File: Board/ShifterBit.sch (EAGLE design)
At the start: 10 parts, among them P1 PINHD-1X10, P2 PINHD-1X10

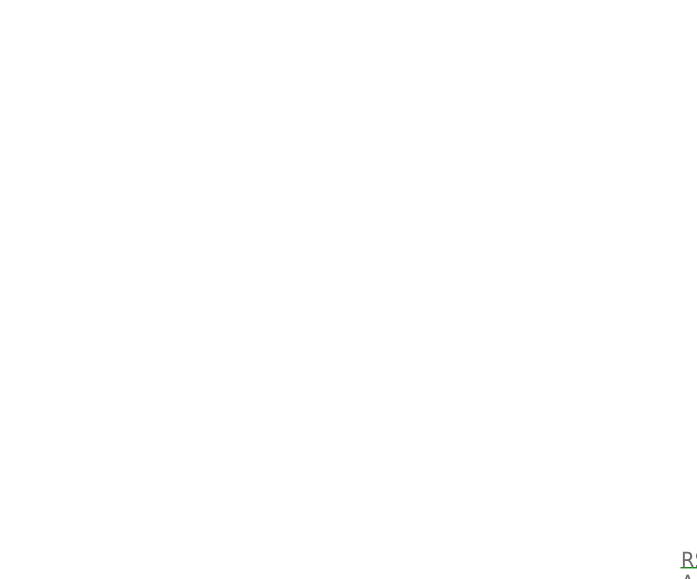
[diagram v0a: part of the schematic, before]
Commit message: renamed and added voltage divider for signal input
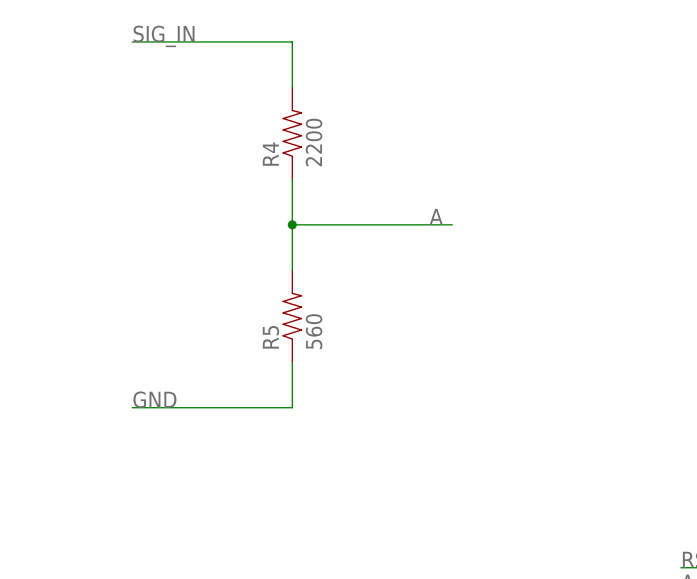
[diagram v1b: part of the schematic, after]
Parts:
- added R4: 2200, SparkFun-Passives:RESISTOR0603-RES
- added R5: 560, SparkFun-Passives:RESISTOR0603-RES
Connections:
- net A: now also R4.1, R5.2
- net GND: now also R5.1
- net SIG_IN: now also R4.2
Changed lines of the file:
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@@
 <part name="R2" library="SparkFun-Passives" deviceset="RESISTOR" device="0603-RES" value="56"/>
 <part name="R3" library="SparkFun-Passives" deviceset="RESISTOR" device="0603-RES" value="56"/>
+<part name="R4" library="SparkFun-Passives" deviceset="RESISTOR" device="0603-RES" value="2200"/>
+<part name="R5" library="SparkFun-Passives" deviceset="RESISTOR" device="0603-RES" value="560"/>
 </parts>
 <sheets>
@@
 <instance part="R2" gate="G$1" x="30.48" y="116.84"/>
 <instance part="R3" gate="G$1" x="182.88" y="114.3"/>
+<instance part="R4" gate="G$1" x="45.72" y="172.72" rot="R90"/>
+<instance part="R5" gate="G$1" x="45.72" y="152.4" rot="R90"/>
 </instances>
 <busses>
@@
 <label x="213.36" y="114.3" size="1.778" layer="95"/>
 </segment>
+<segment>
+<pinref part="R5" gate="G$1" pin="1"/>
+<wire x1="45.72" y1="147.32" x2="45.72" y2="142.24" width="0.1524" layer="91"/>
+<wire x1="45.72" y1="142.24" x2="27.94" y2="142.24" width="0.1524" layer="91"/>
+<label x="27.94" y="142.24" size="1.778" layer="95"/>
+</segment>
 </net>
 <net name="VCC" class="0">
@@
 <label x="45.72" y="60.96" size="1.778" layer="95" rot="R90"/>
 </segment>
+<segment>
+<pinref part="R4" gate="G$1" pin="2"/>
+<wire x1="45.72" y1="177.8" x2="45.72" y2="182.88" width="0.1524" layer="91"/>
+<wire x1="45.72" y1="182.88" x2="27.94" y2="182.88" width="0.1524" layer="91"/>
+<label x="27.94" y="182.88" size="1.778" layer="95"/>
+</segment>
 </net>
 <net name="RST" class="0">
@@
 <label x="88.9" y="121.92" size="1.778" layer="95"/>
 </segment>
+<segment>
+<pinref part="R5" gate="G$1" pin="2"/>
+<pinref part="R4" gate="G$1" pin="1"/>
+<wire x1="45.72" y1="157.48" x2="45.72" y2="162.56" width="0.1524" layer="91"/>
+<wire x1="45.72" y1="162.56" x2="45.72" y2="167.64" width="0.1524" layer="91"/>
+<wire x1="45.72" y1="162.56" x2="63.5" y2="162.56" width="0.1524" layer="91"/>
+<junction x="45.72" y="162.56"/>
+<label x="60.96" y="162.56" size="1.778" layer="95"/>
+</segment>
 </net>

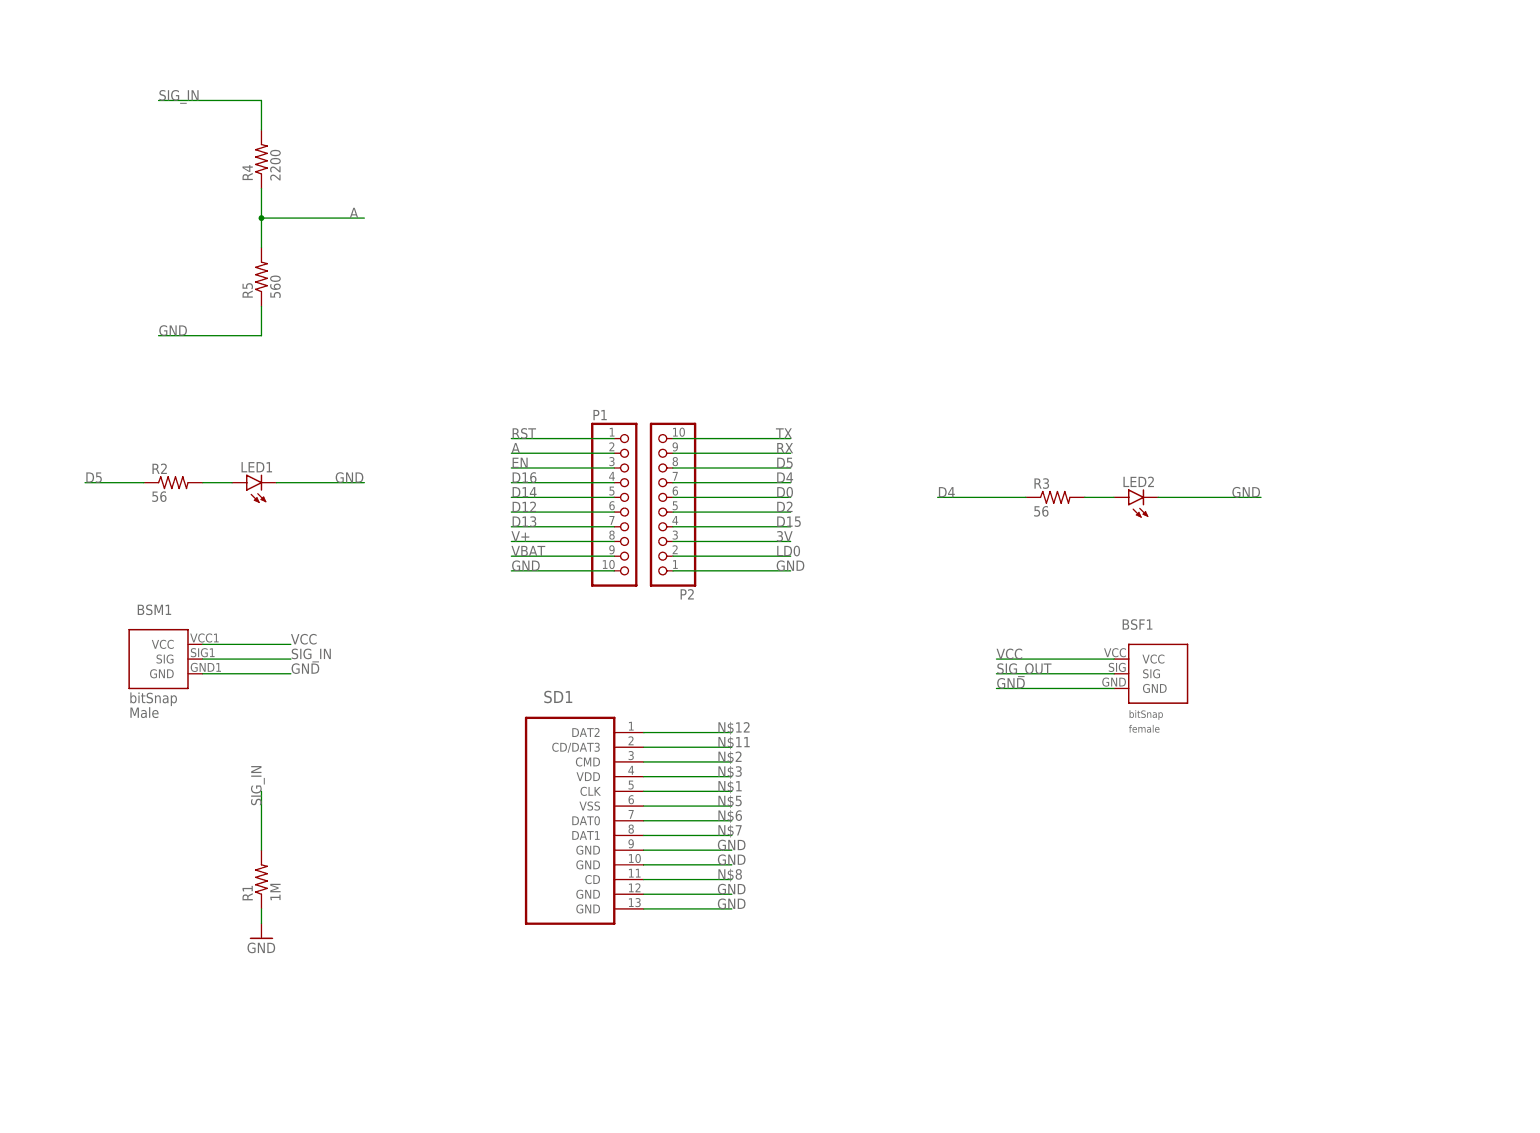
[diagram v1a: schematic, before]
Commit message: added transistor and some labels
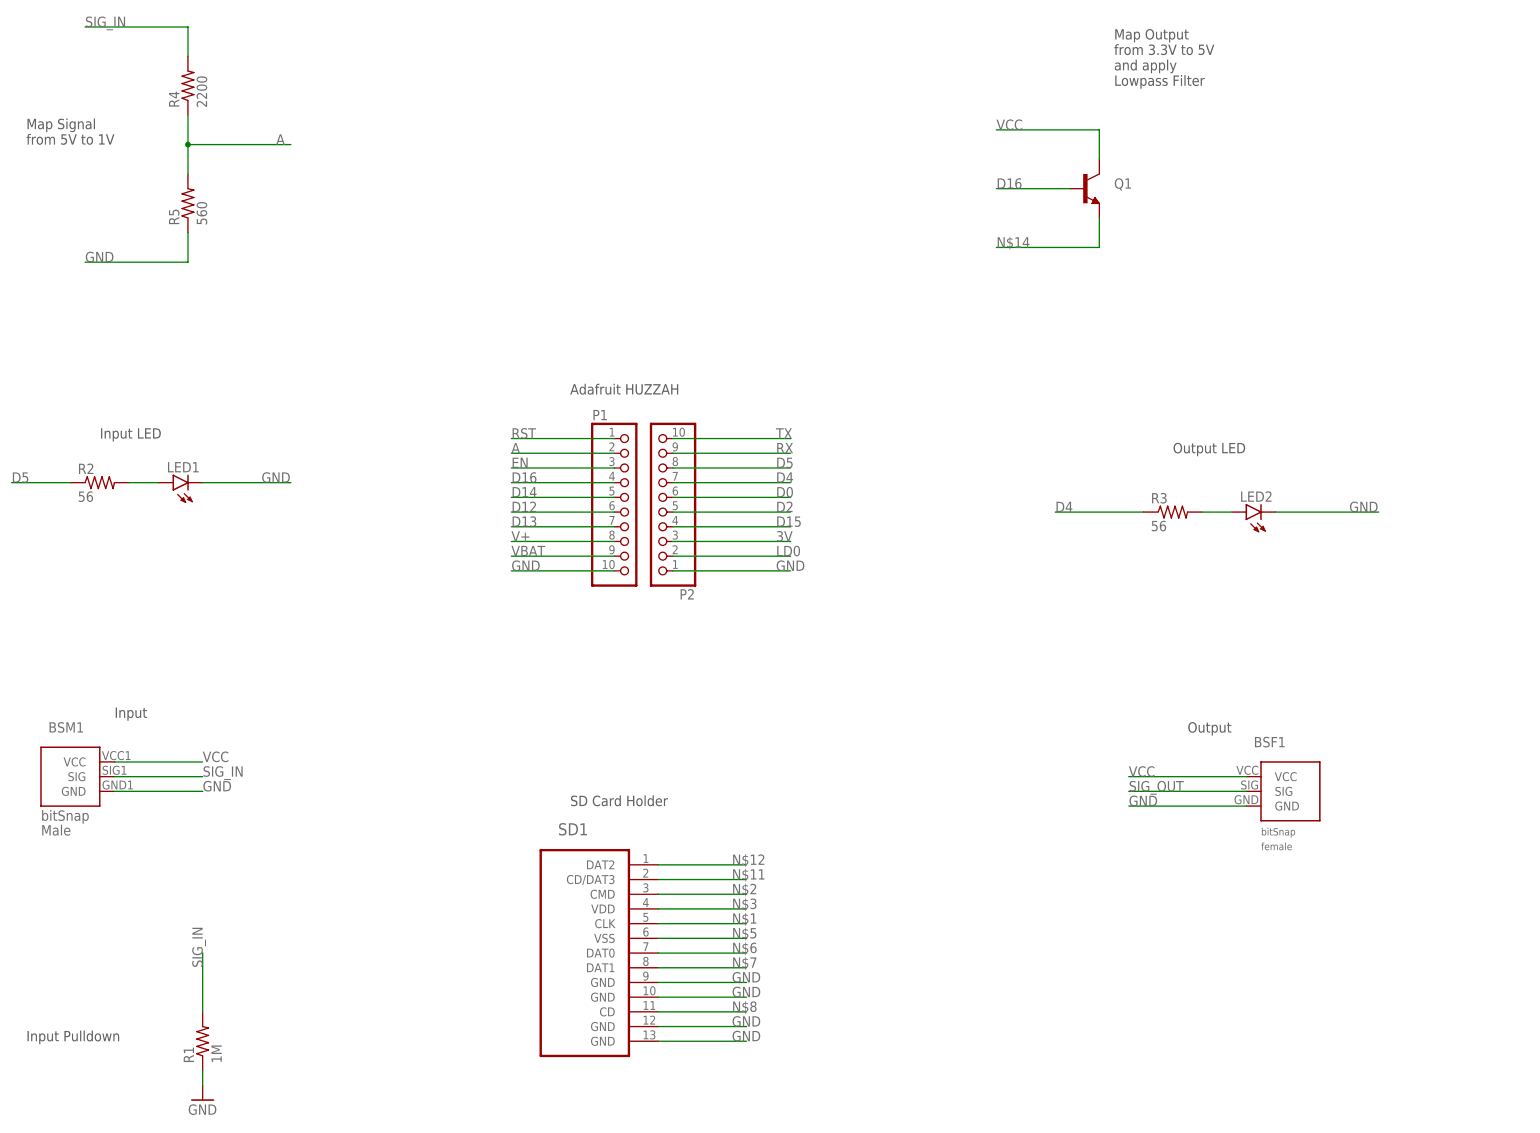
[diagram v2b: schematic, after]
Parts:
- added Q1: (no value), SparkFun-DiscreteSemi:TRANSISTOR_NPNBC547
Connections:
- new net N$14: Q1.E
- net D16: now also Q1.B
- net VCC: now also Q1.C
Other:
- note added: "Adafruit HUZZAH"
- note added: "Input"
- note added: "Input LED"
- note added: "Input Pulldown"
- note added: "Map Output from 3.3V to 5V and apply Lowpass Filter"
- note added: "Map Signal from 5V to 1V"
- note added: "Output"
- note added: "Output LED"
- note added: "SD Card Holder"
- moved on the sheet: BSF1, BSM1, LED1, LED2, R1, R2, R3, R4, R5, SD1

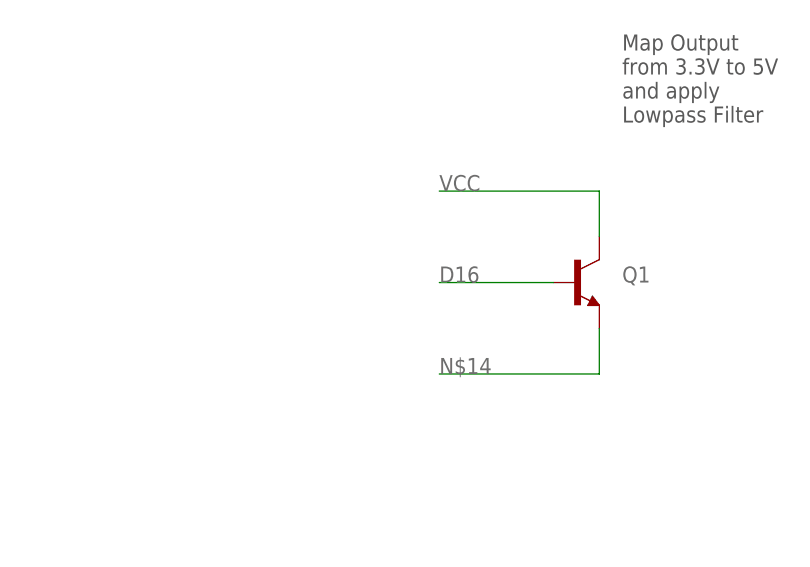
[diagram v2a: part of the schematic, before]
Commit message: added resistor to dac
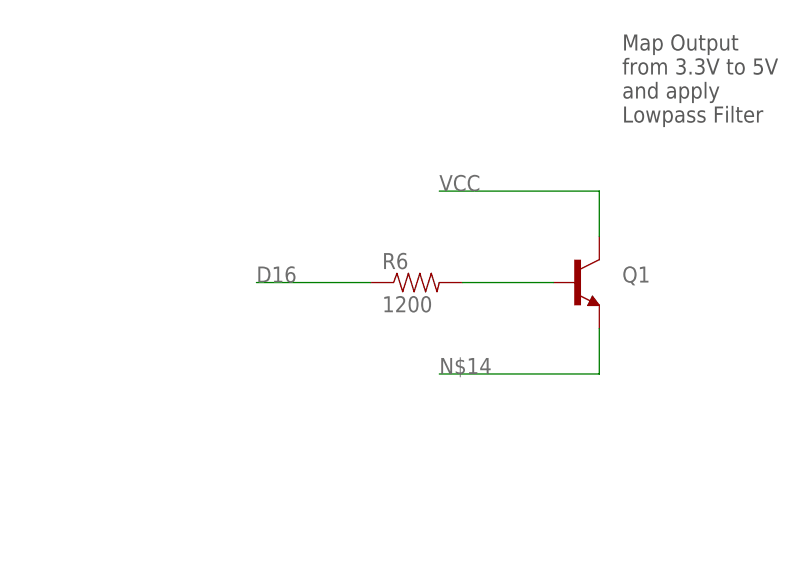
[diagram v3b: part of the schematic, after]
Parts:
- added R6: 1200, SparkFun-Resistors:RESISTOR0603
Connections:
- new net N$10: Q1.B, R6.2
- net D16: now also R6.1; no longer Q1.B
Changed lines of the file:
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@@
 <layer number="227" name="227bmp" color="7" fill="1" visible="yes" active="yes"/>
 <layer number="228" name="228bmp" color="7" fill="1" visible="yes" active="yes"/>
+<layer number="229" name="229bmp" color="7" fill="1" visible="yes" active="yes"/>
+<layer number="230" name="230bmp" color="7" fill="1" visible="yes" active="yes"/>
 <layer number="231" name="Eagle3D_PG1" color="7" fill="1" visible="no" active="no"/>
 <layer number="232" name="Eagle3D_PG2" color="7" fill="1" visible="no" active="no"/>
@@
 <part name="R5" library="SparkFun-Passives" deviceset="RESISTOR" device="0603-RES" value="560"/>
 <part name="Q1" library="SparkFun-DiscreteSemi" deviceset="TRANSISTOR_NPN" device="BC547"/>
+<part name="R6" library="SparkFun-Resistors" deviceset="RESISTOR" device="0603" value="1200"/>
 </parts>
 <sheets>
@@
 <instance part="R5" gate="G$1" x="33.02" y="165.1" rot="R90"/>
 <instance part="Q1" gate="G$1" x="187.96" y="167.64"/>
+<instance part="R6" gate="G$1" x="170.18" y="167.64"/>
 </instances>
 <busses>
@@
 </segment>
 <segment>
-<pinref part="Q1" gate="G$1" pin="B"/>
-<wire x1="185.42" y1="167.64" x2="172.72" y2="167.64" width="0.1524" layer="91"/>
-<label x="172.72" y="167.64" size="1.778" layer="95"/>
+<pinref part="R6" gate="G$1" pin="1"/>
+<wire x1="165.1" y1="167.64" x2="152.4" y2="167.64" width="0.1524" layer="91"/>
+<label x="152.4" y="167.64" size="1.778" layer="95"/>
 </segment>
 </net>
@@
 </segment>
 </net>
+<net name="N$10" class="0">
+<segment>
+<pinref part="R6" gate="G$1" pin="2"/>
+<pinref part="Q1" gate="G$1" pin="B"/>
+<wire x1="175.26" y1="167.64" x2="185.42" y2="167.64" width="0.1524" layer="91"/>
+</segment>
+</net>

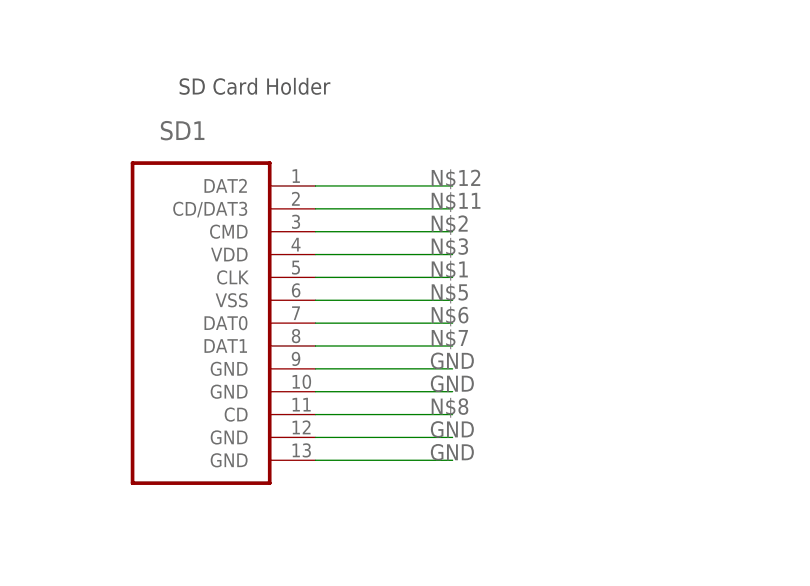
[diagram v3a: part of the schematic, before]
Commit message: connected the sd card
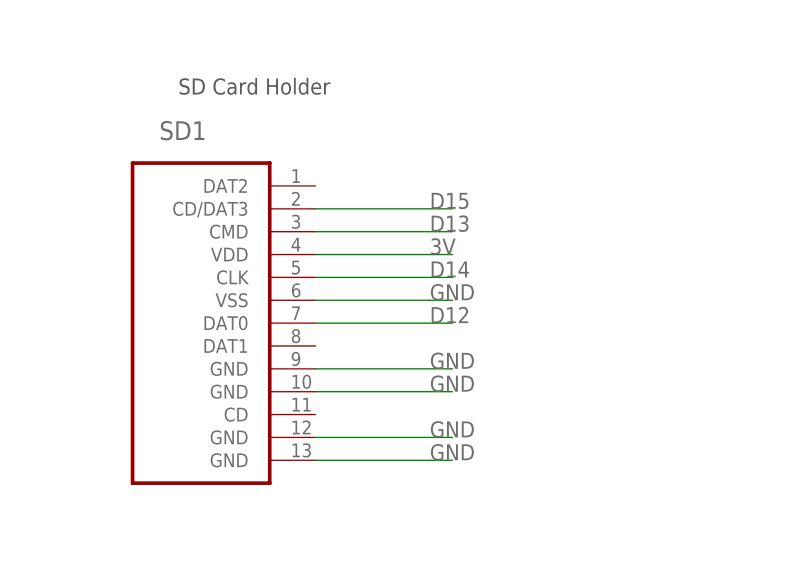
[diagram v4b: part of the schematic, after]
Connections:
- removed net N$1: SD1.CLK
- removed net N$11: SD1.CD/DAT3
- removed net N$12: SD1.DAT2
- removed net N$2: SD1.CMD
- removed net N$3: SD1.VDD
- removed net N$5: SD1.VSS
- removed net N$6: SD1.DAT0
- removed net N$7: SD1.DAT1
- removed net N$8: SD1.CD
- net 3V: now also SD1.VDD
- net D12: now also SD1.DAT0
- net D13: now also SD1.CMD
- net D14: now also SD1.CLK
- net D15: now also SD1.CD/DAT3
- net GND: now also SD1.VSS
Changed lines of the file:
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@@
 <label x="15.24" y="154.94" size="1.778" layer="95"/>
+</segment>
+<segment>
+<pinref part="SD1" gate="A" pin="VSS"/>
+<wire x1="114.3" y1="38.1" x2="129.54" y2="38.1" width="0.1524" layer="91"/>
+<label x="127" y="38.1" size="1.778" layer="95"/>
 </segment>
 </net>
@@
 <label x="88.9" y="114.3" size="1.778" layer="95"/>
 </segment>
+<segment>
+<pinref part="SD1" gate="A" pin="CLK"/>
+<wire x1="114.3" y1="40.64" x2="129.54" y2="40.64" width="0.1524" layer="91"/>
+<label x="127" y="40.64" size="1.778" layer="95"/>
+</segment>
 </net>
 <net name="D12" class="0">
@@
 <label x="88.9" y="111.76" size="1.778" layer="95"/>
 </segment>
+<segment>
+<pinref part="SD1" gate="A" pin="DAT0"/>
+<wire x1="114.3" y1="35.56" x2="129.54" y2="35.56" width="0.1524" layer="91"/>
+<label x="127" y="35.56" size="1.778" layer="95"/>
+</segment>
 </net>
 <net name="D13" class="0">
@@
 <label x="88.9" y="109.22" size="1.778" layer="95"/>
 </segment>
+<segment>
+<pinref part="SD1" gate="A" pin="CMD"/>
+<wire x1="114.3" y1="45.72" x2="129.54" y2="45.72" width="0.1524" layer="91"/>
+<label x="127" y="45.72" size="1.778" layer="95"/>
+</segment>
 </net>
 <net name="V+" class="0">
@@
 <label x="134.62" y="109.22" size="1.778" layer="95"/>
 </segment>
+<segment>
+<pinref part="SD1" gate="A" pin="CD/DAT3"/>
+<wire x1="114.3" y1="48.26" x2="129.54" y2="48.26" width="0.1524" layer="91"/>
+<label x="127" y="48.26" size="1.778" layer="95"/>
+</segment>
 </net>
 <net name="3V" class="0">
@@
 <label x="134.62" y="106.68" size="1.778" layer="95"/>
 </segment>
+<segment>
+<pinref part="SD1" gate="A" pin="VDD"/>
+<wire x1="114.3" y1="43.18" x2="129.54" y2="43.18" width="0.1524" layer="91"/>
+<label x="127" y="43.18" size="1.778" layer="95"/>
+</segment>
 </net>
 <net name="LD0" class="0">
@@
 </segment>
 </net>
-<net name="N$1" class="0">
-<segment>
-<pinref part="SD1" gate="A" pin="CLK"/>
-<wire x1="114.3" y1="40.64" x2="129.54" y2="40.64" width="0.1524" layer="91"/>
-<label x="127" y="40.64" size="1.778" layer="95"/>
-</segment>
-</net>
-<net name="N$2" class="0">
-<segment>
-<pinref part="SD1" gate="A" pin="CMD"/>
-<wire x1="114.3" y1="45.72" x2="129.54" y2="45.72" width="0.1524" layer="91"/>
-<label x="127" y="45.72" size="1.778" layer="95"/>
-</segment>
-</net>
-<net name="N$3" class="0">
-<segment>
-<pinref part="SD1" gate="A" pin="VDD"/>
-<wire x1="114.3" y1="43.18" x2="129.54" y2="43.18" width="0.1524" layer="91"/>
-<label x="127" y="43.18" size="1.778" layer="95"/>
-</segment>
-</net>
-<net name="N$5" class="0">
-<segment>
-<pinref part="SD1" gate="A" pin="VSS"/>
-<wire x1="114.3" y1="38.1" x2="129.54" y2="38.1" width="0.1524" layer="91"/>
-<label x="127" y="38.1" size="1.778" layer="95"/>
-</segment>
-</net>
-<net name="N$6" class="0">
-<segment>
-<pinref part="SD1" gate="A" pin="DAT0"/>
-<wire x1="114.3" y1="35.56" x2="129.54" y2="35.56" width="0.1524" layer="91"/>
-<label x="127" y="35.56" size="1.778" layer="95"/>
-</segment>
-</net>
-<net name="N$7" class="0">
-<segment>
-<pinref part="SD1" gate="A" pin="DAT1"/>
-<wire x1="114.3" y1="33.02" x2="129.54" y2="33.02" width="0.1524" layer="91"/>
-<label x="127" y="33.02" size="1.778" layer="95"/>
-</segment>
-</net>
-<net name="N$8" class="0">
-<segment>
-<pinref part="SD1" gate="A" pin="CD"/>
-<wire x1="114.3" y1="25.4" x2="129.54" y2="25.4" width="0.1524" layer="91"/>
-<label x="127" y="25.4" size="1.778" layer="95"/>
-</segment>
-</net>
-<net name="N$11" class="0">
-<segment>
-<pinref part="SD1" gate="A" pin="CD/DAT3"/>
-<wire x1="114.3" y1="48.26" x2="129.54" y2="48.26" width="0.1524" layer="91"/>
-<label x="127" y="48.26" size="1.778" layer="95"/>
-</segment>
-</net>
-<net name="N$12" class="0">
-<segment>
-<pinref part="SD1" gate="A" pin="DAT2"/>
-<wire x1="114.3" y1="50.8" x2="129.54" y2="50.8" width="0.1524" layer="91"/>
-<label x="127" y="50.8" size="1.778" layer="95"/>
-</segment>
-</net>
